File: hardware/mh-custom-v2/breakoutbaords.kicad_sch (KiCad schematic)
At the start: 8 parts, among them J3 Conn_02x19_Top_Bottom, J4 Conn_02x19_Top_Bottom

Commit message: approaching ordering from JLCPCB
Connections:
- net ade7953-reset: now also J3.17 (Pin_17), J3.18 (Pin_18); no longer J4.19 (Pin_19), J4.20 (Pin_20)
- net buzz: now also J4.19 (Pin_19), J4.20 (Pin_20); no longer J3.17 (Pin_17), J3.18 (Pin_18)
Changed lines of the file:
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@@
   (junction (at 111.76 129.54) (diameter 0) (color 0 0 0 0)
   )
+  (junction (at 111.76 144.78) (diameter 0) (color 0 0 0 0)
+  )
   (junction (at 207.01 92.71) (diameter 0) (color 0 0 0 0)
   )
@@
   (junction (at 111.76 157.48) (diameter 0) (color 0 0 0 0)
   )
+  (junction (at 111.76 142.24) (diameter 0) (color 0 0 0 0)
+  )
+  (junction (at 71.12 162.56) (diameter 0) (color 0 0 0 0)
+  )
+  (junction (at 87.63 35.56) (diameter 0) (color 0 0 0 0)
+  )
+  (junction (at 71.12 132.08) (diameter 0) (color 0 0 0 0)
+  )
   (junction (at 71.12 142.24) (diameter 0) (color 0 0 0 0)
   )
-  (junction (at 111.76 142.24) (diameter 0) (color 0 0 0 0)
-  )
-  (junction (at 71.12 162.56) (diameter 0) (color 0 0 0 0)
-  )
-  (junction (at 87.63 35.56) (diameter 0) (color 0 0 0 0)
-  )
-  (junction (at 71.12 132.08) (diameter 0) (color 0 0 0 0)
-  )
   (junction (at 111.76 167.64) (diameter 0) (color 0 0 0 0)
   )
@@
   (junction (at 111.76 147.32) (diameter 0) (color 0 0 0 0)
   )
-  (junction (at 111.76 144.78) (diameter 0) (color 0 0 0 0)
-  )
   (junction (at 111.76 132.08) (diameter 0) (color 0 0 0 0)
   )
@@
     (stroke (width 0) (type default) (color 0 0 0 0))
   )
+  (wire (pts (xy 111.76 144.78) (xy 113.03 144.78))
+    (stroke (width 0) (type default) (color 0 0 0 0))
+  )
   (wire (pts (xy 99.06 162.56) (xy 111.76 162.56))
     (stroke (width 0) (type default) (color 0 0 0 0))
@@
     (stroke (width 0) (type default) (color 0 0 0 0))
   )
+  (wire (pts (xy 69.85 142.24) (xy 71.12 142.24))
+    (stroke (width 0) (type default) (color 0 0 0 0))
+  )
   (wire (pts (xy 99.06 144.78) (xy 111.76 144.78))
     (stroke (width 0) (type default) (color 0 0 0 0))
@@
     (stroke (width 0) (type default) (color 0 0 0 0))
   )
-  (wire (pts (xy 111.76 144.78) (xy 113.03 144.78))
-    (stroke (width 0) (type default) (color 0 0 0 0))
-  )
   (wire (pts (xy 217.17 90.17) (xy 217.17 91.44))
     (stroke (width 0) (type default) (color 0 0 0 0))
@@
   )
   (wire (pts (xy 111.76 142.24) (xy 113.03 142.24))
-    (stroke (width 0) (type default) (color 0 0 0 0))
-  )
-  (wire (pts (xy 69.85 142.24) (xy 71.12 142.24))
     (stroke (width 0) (type default) (color 0 0 0 0))
   )
@@
     )
   )
-  (global_label "buzz" (shape output) (at 69.85 142.24 180) (fields_autoplaced)
-    (effects (font (size 1.27 1.27)) (justify right))
-    (property "Intersheet References" "${INTERSHEET_REFS}" (id 0) (at 63.0826 142.3194 0)
-      (effects (font (size 1.27 1.27)) (justify right) hide)
+  (global_label "buzz" (shape output) (at 113.03 144.78 0) (fields_autoplaced)
+    (effects (font (size 1.27 1.27)) (justify left))
+    (property "Intersheet References" "${INTERSHEET_REFS}" (id 0) (at 119.7974 144.7006 0)
+      (effects (font (size 1.27 1.27)) (justify left) hide)
     )
   )
@@
     )
   )
-  (global_label "ade7953-reset" (shape input) (at 113.03 144.78 0) (fields_autoplaced)
-    (effects (font (size 1.27 1.27)) (justify left))
-    (property "Intersheet References" "${INTERSHEET_REFS}" (id 0) (at 129.9574 144.8594 0)
-      (effects (font (size 1.27 1.27)) (justify left) hide)
-    )
-  )
+  (global_label "ade7953-reset" (shape input) (at 69.85 142.24 180) (fields_autoplaced)
+    (effects (font (size 1.27 1.27)) (justify right))
+    (property "Intersheet References" "${INTERSHEET_REFS}" (id 0) (at 52.9226 142.1606 0)
+      (effects (font (size 1.27 1.27)) (justify right) hide)
+    )
+  )

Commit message: prepping for JLCPCB order - all parts listed with numbers, BOM generated
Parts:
- I2C-1, I2C-2, I2C-3: JLCPCB Part # (none) -> C131334
- R7, R8: JLCPCB Part # (none) -> C25804
- SPI-1: JLCPCB Part # (none) -> C131342
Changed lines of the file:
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@@
+      (effects (font (size 1.27 1.27)) hide)
+    )
+    (property "JLCPCB Part #" "C25804" (id 4) (at 91.44 39.37 0)
       (effects (font (size 1.27 1.27)) hide)
     )
@@
     )
     (property "Datasheet" "~" (id 3) (at 223.52 85.09 0)
+      (effects (font (size 1.27 1.27)) hide)
+    )
+    (property "JLCPCB Part #" "C131342" (id 4) (at 223.52 85.09 0)
       (effects (font (size 1.27 1.27)) hide)
     )
@@
       (effects (font (size 1.27 1.27)) hide)
     )
+    (property "JLCPCB Part #" "C131334" (id 4) (at 102.87 64.77 0)
+      (effects (font (size 1.27 1.27)) hide)
+    )
     (pin "1")
     (pin "2")
@@
     )
     (property "Datasheet" "~" (id 3) (at 102.87 82.55 0)
+      (effects (font (size 1.27 1.27)) hide)
+    )
+    (property "JLCPCB Part #" "C131334" (id 4) (at 102.87 82.55 0)
       (effects (font (size 1.27 1.27)) hide)
     )
@@
       (effects (font (size 1.27 1.27)) hide)
     )
+    (property "JLCPCB Part #" "C25804" (id 4) (at 87.63 39.37 0)
+      (effects (font (size 1.27 1.27)) hide)
+    )
     (pin "1")
     (pin "2")
@@
       (effects (font (size 1.27 1.27)) hide)
     )
+    (property "JLCPCB Part #" "C131334" (id 4) (at 102.87 46.99 0)
+      (effects (font (size 1.27 1.27)) hide)
+    )

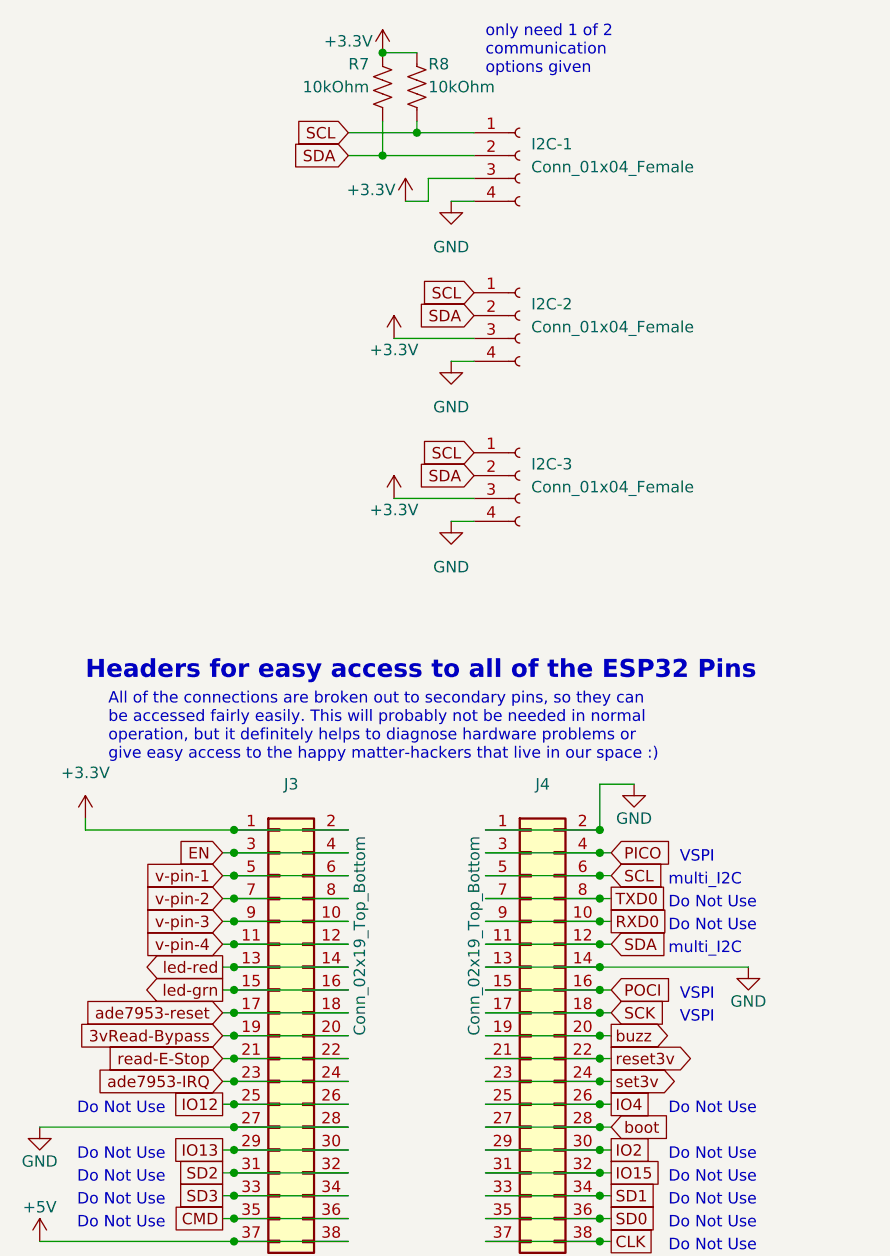
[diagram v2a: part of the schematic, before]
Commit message: improved some of the connections for easier soldering/production
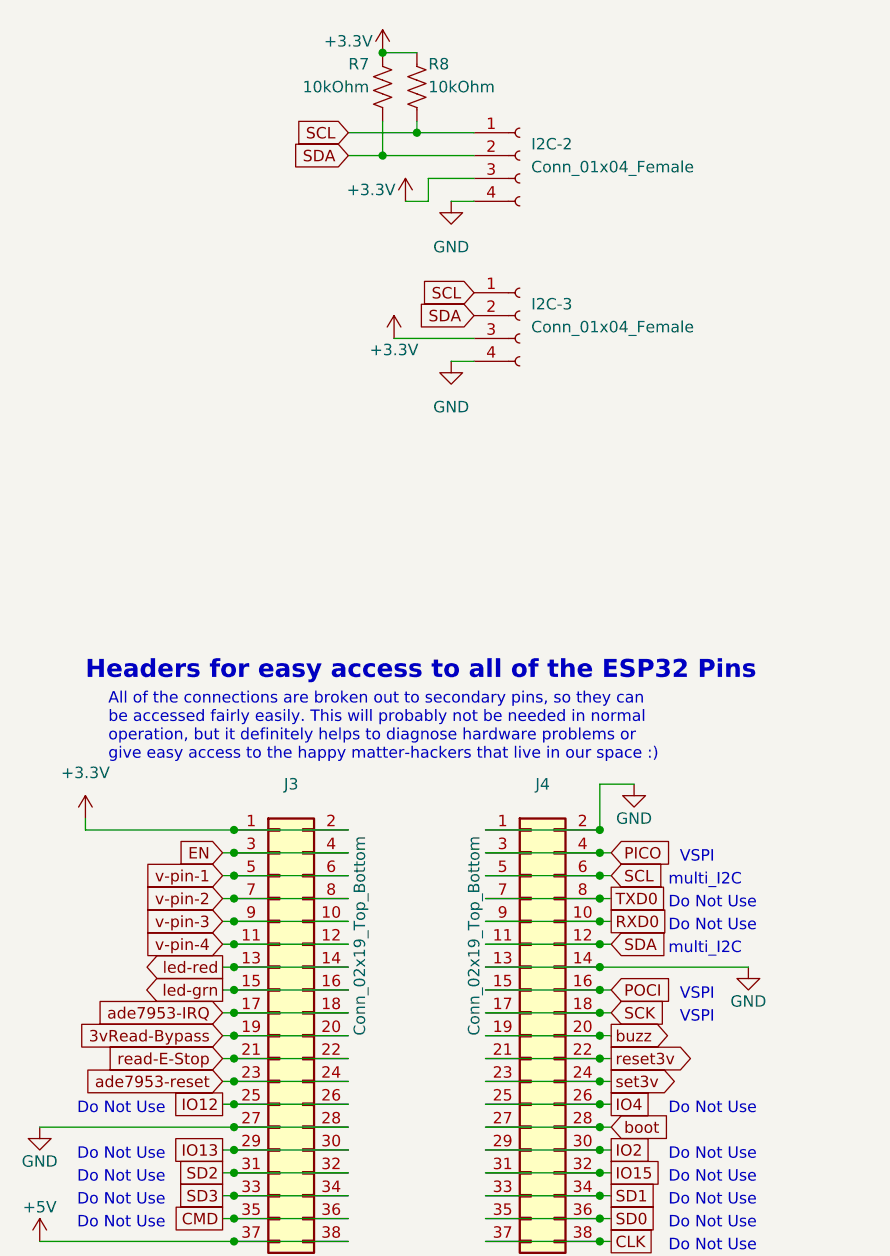
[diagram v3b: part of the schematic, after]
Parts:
- removed I2C-1: Conn_01x04_Female, Connector_JST:JST_PH_B4B-PH-K_1x04_P2.00mm_Vertical, symbol Connector:Conn_01x04_Female
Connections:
- net ade7953-IRQ: now also J3.17 (Pin_17), J3.18 (Pin_18); no longer J3.23 (Pin_23), J3.24 (Pin_24)
- net ade7953-reset: now also J3.23 (Pin_23), J3.24 (Pin_24); no longer J3.17 (Pin_17), J3.18 (Pin_18)
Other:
- note removed: "only need 1 of 2 communication options given"
- moved on the sheet: I2C-2, I2C-3

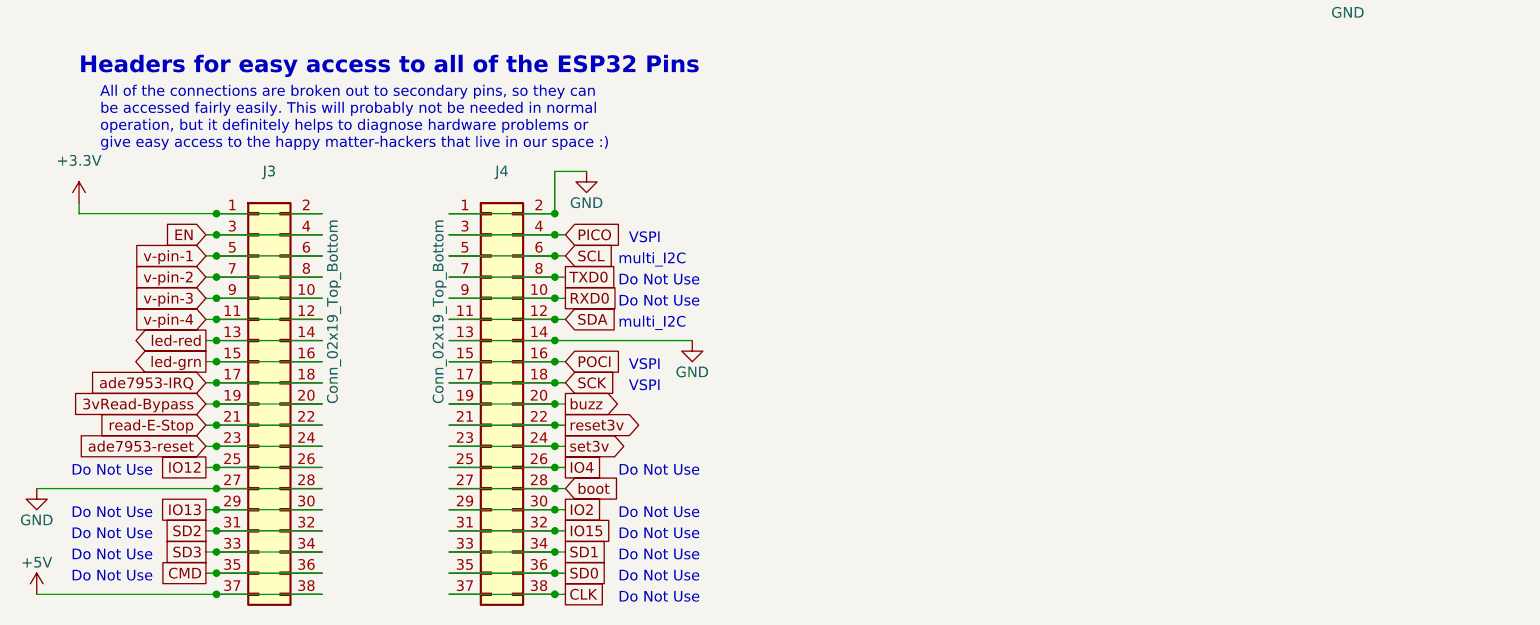
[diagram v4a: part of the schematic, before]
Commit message: added linear regulator for 3.3V peripherals and ADE7953 reset jumper
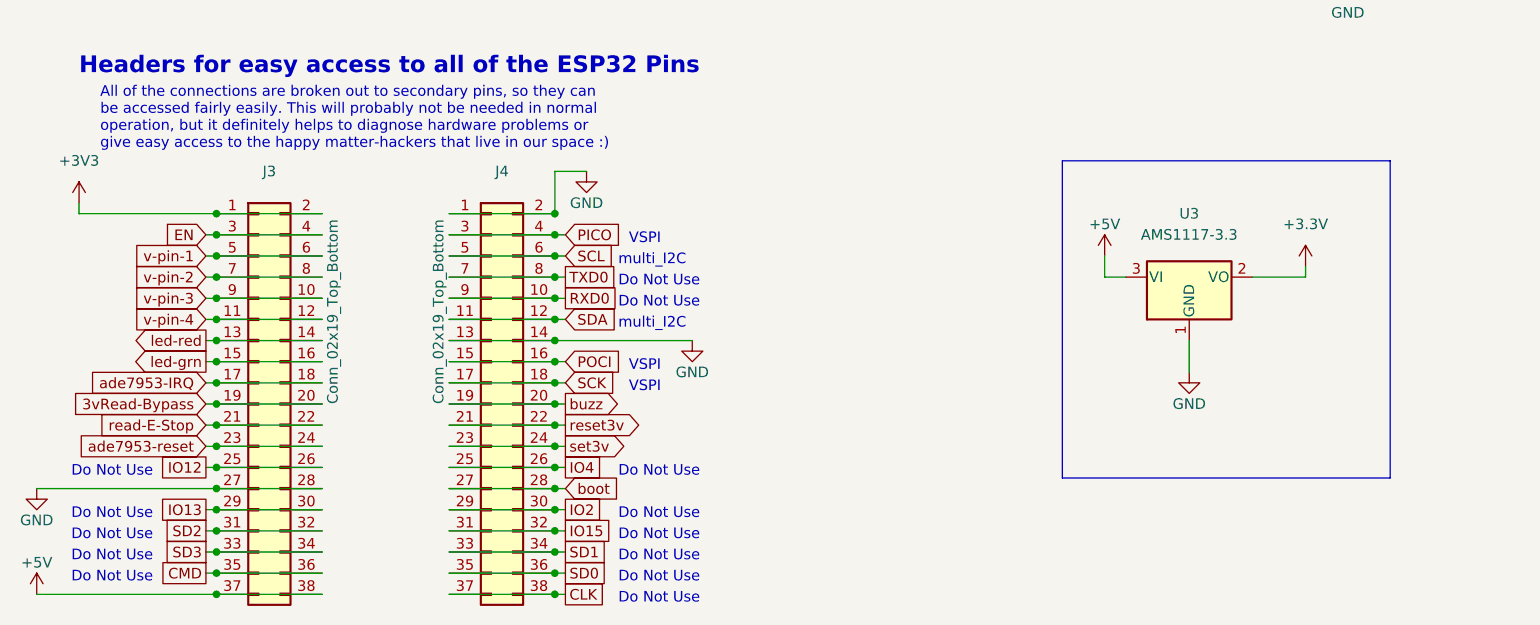
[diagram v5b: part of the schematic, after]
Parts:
- added U3: AMS1117-3.3, Package_TO_SOT_SMD:SOT-223-3_TabPin2, symbol Regulator_Linear:AMS1117-3.3
- R7, R8: now left out of the parts list
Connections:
- net +3V3: now also U3.2 (VO)
- net +5V: now also U3.3 (VI)
- net GND: now also U3.1 (GND)
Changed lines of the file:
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@@
+    (stroke (width 0) (type default) (color 0 0 0 0))
+  )
+  (polyline (pts (xy 172.72 115.57) (xy 172.72 153.67))
     (stroke (width 0) (type default) (color 0 0 0 0))
   )
@@
     (stroke (width 0) (type default) (color 0 0 0 0))
   )
+  (wire (pts (xy 201.93 129.54) (xy 201.93 128.27))
+    (stroke (width 0) (type default) (color 0 0 0 0))
+  )
   (wire (pts (xy 111.76 165.1) (xy 113.03 165.1))
     (stroke (width 0) (type default) (color 0 0 0 0))
   )
+  (polyline (pts (xy 212.09 153.67) (xy 172.72 153.67))
+    (stroke (width 0) (type default) (color 0 0 0 0))
+  )
+  (polyline (pts (xy 172.72 115.57) (xy 212.09 115.57))
+    (stroke (width 0) (type default) (color 0 0 0 0))
+  )
   (wire (pts (xy 71.12 129.54) (xy 83.82 129.54))
     (stroke (width 0) (type default) (color 0 0 0 0))
@@
     (stroke (width 0) (type default) (color 0 0 0 0))
   )
+  (wire (pts (xy 187.96 137.16) (xy 187.96 140.97))
+    (stroke (width 0) (type default) (color 0 0 0 0))
+  )
   (wire (pts (xy 69.85 160.02) (xy 71.12 160.02))
     (stroke (width 0) (type default) (color 0 0 0 0))
@@
     (stroke (width 0) (type default) (color 0 0 0 0))
   )
+  (wire (pts (xy 177.8 127) (xy 177.8 129.54))
+    (stroke (width 0) (type default) (color 0 0 0 0))
+  )
   (wire (pts (xy 91.44 43.18) (xy 91.44 44.45))
     (stroke (width 0) (type default) (color 0 0 0 0))
@@
     (stroke (width 0) (type default) (color 0 0 0 0))
   )
+  (wire (pts (xy 177.8 129.54) (xy 180.34 129.54))
+    (stroke (width 0) (type default) (color 0 0 0 0))
+  )
   (wire (pts (xy 71.12 142.24) (xy 83.82 142.24))
     (stroke (width 0) (type default) (color 0 0 0 0))
@@
     (stroke (width 0) (type default) (color 0 0 0 0))
   )
+  (polyline (pts (xy 212.09 115.57) (xy 212.09 153.67))
+    (stroke (width 0) (type default) (color 0 0 0 0))
+  )
   (wire (pts (xy 87.63 43.18) (xy 87.63 46.99))
     (stroke (width 0) (type default) (color 0 0 0 0))
@@
   )
   (wire (pts (xy 71.12 121.92) (xy 83.82 121.92))
+    (stroke (width 0) (type default) (color 0 0 0 0))
+  )
+  (wire (pts (xy 195.58 129.54) (xy 201.93 129.54))
     (stroke (width 0) (type default) (color 0 0 0 0))
   )
@@
   )
   (symbol (lib_id "Device:R_US") (at 91.44 39.37 180) (unit 1)
-    (in_bom yes) (on_board yes)
+    (in_bom no) (on_board yes)
     (property "Reference" "R8" (id 0) (at 92.71 36.83 0)
       (effects (font (size 1.27 1.27)) (justify right))
@@
     (pin "6")
   )
+  (symbol (lib_id "power:GND") (at 187.96 140.97 0) (unit 1)
+    (in_bom yes) (on_board yes)
+    (property "Reference" "#PWR07" (id 0) (at 187.96 147.32 0)
+      (effects (font (size 1.27 1.27)) hide)
+    )
+    (property "Value" "GND" (id 1) (at 187.96 144.78 0))
+    (property "Footprint" "" (id 2) (at 187.96 140.97 0)
+      (effects (font (size 1.27 1.27)) hide)
+    )
+    (property "Datasheet" "" (id 3) (at 187.96 140.97 0)
+      (effects (font (size 1.27 1.27)) hide)
+    )
+    (pin "1")
+  )
+  (symbol (lib_id "power:+5V") (at 177.8 127 0) (unit 1)
+    (in_bom yes) (on_board yes)
+    (property "Reference" "#PWR06" (id 0) (at 177.8 130.81 0)
+      (effects (font (size 1.27 1.27)) hide)
+    )
+    (property "Value" "+5V" (id 1) (at 177.8 123.19 0))
+    (property "Footprint" "" (id 2) (at 177.8 127 0)
+      (effects (font (size 1.27 1.27)) hide)
+    )
+    (property "Datasheet" "" (id 3) (at 177.8 127 0)
+      (effects (font (size 1.27 1.27)) hide)
+    )
+    (pin "1")
+  )
   (symbol (lib_id "power:+3.3V") (at 214.63 91.44 0) (unit 1)
     (in_bom yes) (on_board yes)
@@
     )
     (pin "1")
+  )
+  (symbol (lib_id "Regulator_Linear:AMS1117-3.3") (at 187.96 129.54 0) (unit 1)
+    (in_bom yes) (on_board yes) (fields_autoplaced)
+    (property "Reference" "U3" (id 0) (at 187.96 121.92 0))
+    (property "Value" "AMS1117-3.3" (id 1) (at 187.96 124.46 0))
+    (property "Footprint" "Package_TO_SOT_SMD:SOT-223-3_TabPin2" (id 2) (at 187.96 124.46 0)
+      (effects (font (size 1.27 1.27)) hide)
+    )
+    (property "Datasheet" "http://www.advanced-monolithic.com/pdf/ds1117.pdf" (id 3) (at 190.5 135.89 0)
+      (effects (font (size 1.27 1.27)) hide)
+    )
+    (property "JLCPCB Part #" "C6186" (id 4) (at 187.96 129.54 0)
+      (effects (font (size 1.27 1.27)) hide)
+    )
+    (pin "1")
+    (pin "2")
+    (pin "3")
   )
   (symbol (lib_id "Connector_Generic:Conn_02x19_Odd_Even") (at 104.14 144.78 0) (unit 1)
@@
     (pin "1")
   )
+  (symbol (lib_id "power:+3V3") (at 54.61 120.65 0) (unit 1)
+    (in_bom yes) (on_board yes) (fields_autoplaced)
+    (property "Reference" "#PWR05" (id 0) (at 54.61 124.46 0)
+      (effects (font (size 1.27 1.27)) hide)
+    )
+    (property "Value" "+3V3" (id 1) (at 54.61 115.57 0))
+    (property "Footprint" "" (id 2) (at 54.61 120.65 0)
+      (effects (font (size 1.27 1.27)) hide)
+    )
+    (property "Datasheet" "" (id 3) (at 54.61 120.65 0)
+      (effects (font (size 1.27 1.27)) hide)
+    )
+    (pin "1")
+  )
   (symbol (lib_id "power:GND") (at 115.57 116.84 0) (unit 1)
     (in_bom yes) (on_board yes)
@@
     )
     (property "Datasheet" "" (id 3) (at 128.27 137.16 0)
-      (effects (font (size 1.27 1.27)) hide)
-    )
-    (pin "1")
-  )
-  (symbol (lib_id "power:+3.3V") (at 54.61 120.65 0) (unit 1)
-    (in_bom yes) (on_board yes) (fields_autoplaced)
-    (property "Reference" "#PWR0119" (id 0) (at 54.61 124.46 0)
-      (effects (font (size 1.27 1.27)) hide)
-    )
-    (property "Value" "+3.3V" (id 1) (at 54.61 115.57 0))
-    (property "Footprint" "" (id 2) (at 54.61 120.65 0)
-      (effects (font (size 1.27 1.27)) hide)
-    )
-    (property "Datasheet" "" (id 3) (at 54.61 120.65 0)
       (effects (font (size 1.27 1.27)) hide)
     )
@@
     (pin "9")
   )
+  (symbol (lib_id "power:+3.3V") (at 201.93 128.27 0) (unit 1)
+    (in_bom yes) (on_board yes) (fields_autoplaced)
+    (property "Reference" "#PWR08" (id 0) (at 201.93 132.08 0)
+      (effects (font (size 1.27 1.27)) hide)
+    )
+    (property "Value" "+3.3V" (id 1) (at 201.93 123.19 0))
+    (property "Footprint" "" (id 2) (at 201.93 128.27 0)
+      (effects (font (size 1.27 1.27)) hide)
+    )
+    (property "Datasheet" "" (id 3) (at 201.93 128.27 0)
+      (effects (font (size 1.27 1.27)) hide)
+    )
+    (pin "1")
+  )
   (symbol (lib_id "Device:R_US") (at 87.63 39.37 180) (unit 1)
-    (in_bom yes) (on_board yes)
+    (in_bom no) (on_board yes)
     (property "Reference" "R7" (id 0) (at 83.82 36.83 0)
       (effects (font (size 1.27 1.27)) (justify right))
